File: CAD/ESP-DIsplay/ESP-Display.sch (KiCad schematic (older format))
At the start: 25 parts, among them J101 IO_Conn, J102 Conn_Power, SW101 SW_On, SW102 SW_Down, SW103 SW_Up, SW104 SW_T3, SW105 SW_T2, SW106 SW_T1, U101 SPI-TFT-1-8

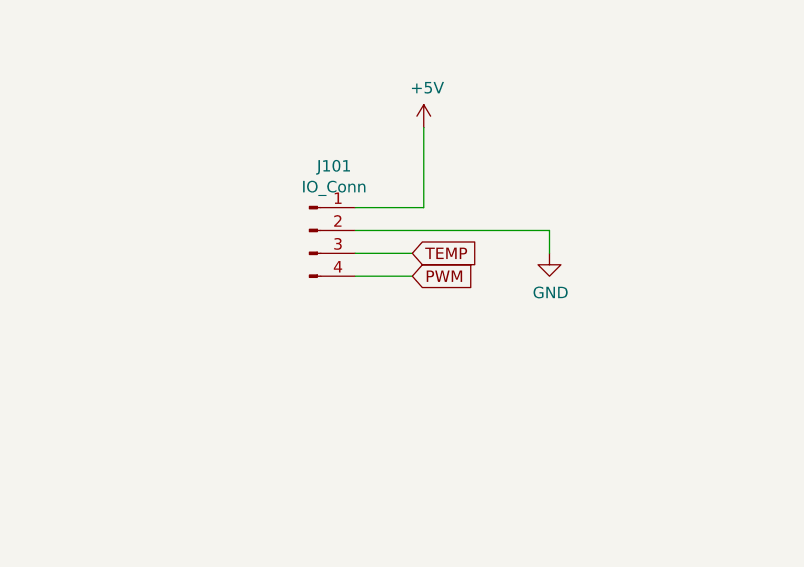
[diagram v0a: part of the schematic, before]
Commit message: esp12e adc pinsadded, 1117 power module
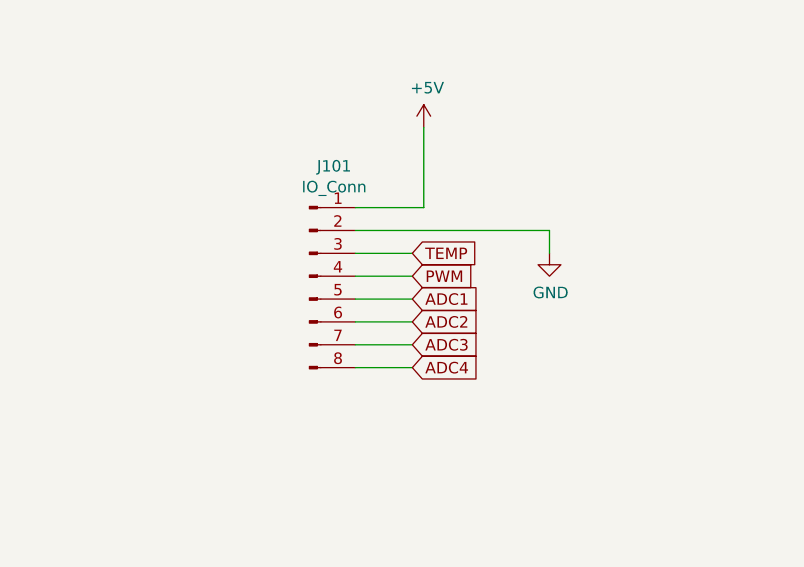
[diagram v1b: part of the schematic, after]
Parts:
- removed J101: IO_Conn, Connector_PinHeader_2.54mm:PinHeader_1x04_P2.54mm_Vertical, symbol Connector:Conn_01x04_Male
- added J101: IO_Conn, Connector_PinHeader_2.54mm:PinHeader_1x08_P2.54mm_Vertical, symbol Connector:Conn_01x08_Male
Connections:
- net labels added: ADC1, ADC2, ADC3, ADC4
- wire segments 65 -> 69
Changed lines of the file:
@@
-$EndComp
-$Comp
-L Connector:Conn_01x04_Male J101
-U 1 1 603BB008
-P 2150 5000
-F 0 "J101" H 2258 5281 50  0000 C CNN
-F 1 "IO_Conn" H 2258 5190 50  0000 C CNN
-F 2 "Connector_PinHeader_2.54mm:PinHeader_1x04_P2.54mm_Vertical" H 2150 5000 50  0001 C CNN
-F 3 "~" H 2150 5000 50  0001 C CNN
-	1    2150 5000
-	1    0    0    -1
 $EndComp
 $Comp
@@
 Wire Wire Line
 	6100 5100 6250 5100
+$Comp
+L Connector:Conn_01x08_Male J101
+U 1 1 603C3897
+P 2150 5200
+F 0 "J101" H 2258 5681 50  0000 C CNN
+F 1 "IO_Conn" H 2258 5590 50  0000 C CNN
+F 2 "Connector_PinHeader_2.54mm:PinHeader_1x08_P2.54mm_Vertical" H 2150 5200 50  0001 C CNN
+F 3 "~" H 2150 5200 50  0001 C CNN
+	1    2150 5200
+	1    0    0    -1
+$EndComp
+Text GLabel 2600 5300 2    50   Input ~ 0
+ADC1
+Text GLabel 2600 5400 2    50   Input ~ 0
+ADC2
+Text GLabel 2600 5500 2    50   Input ~ 0
+ADC3
+Text GLabel 2600 5600 2    50   Input ~ 0
+ADC4
+Wire Wire Line
+	2350 5300 2600 5300
+Wire Wire Line
+	2350 5400 2600 5400
+Wire Wire Line
+	2350 5500 2600 5500
+Wire Wire Line
+	2350 5600 2600 5600
 $EndSCHEMATC

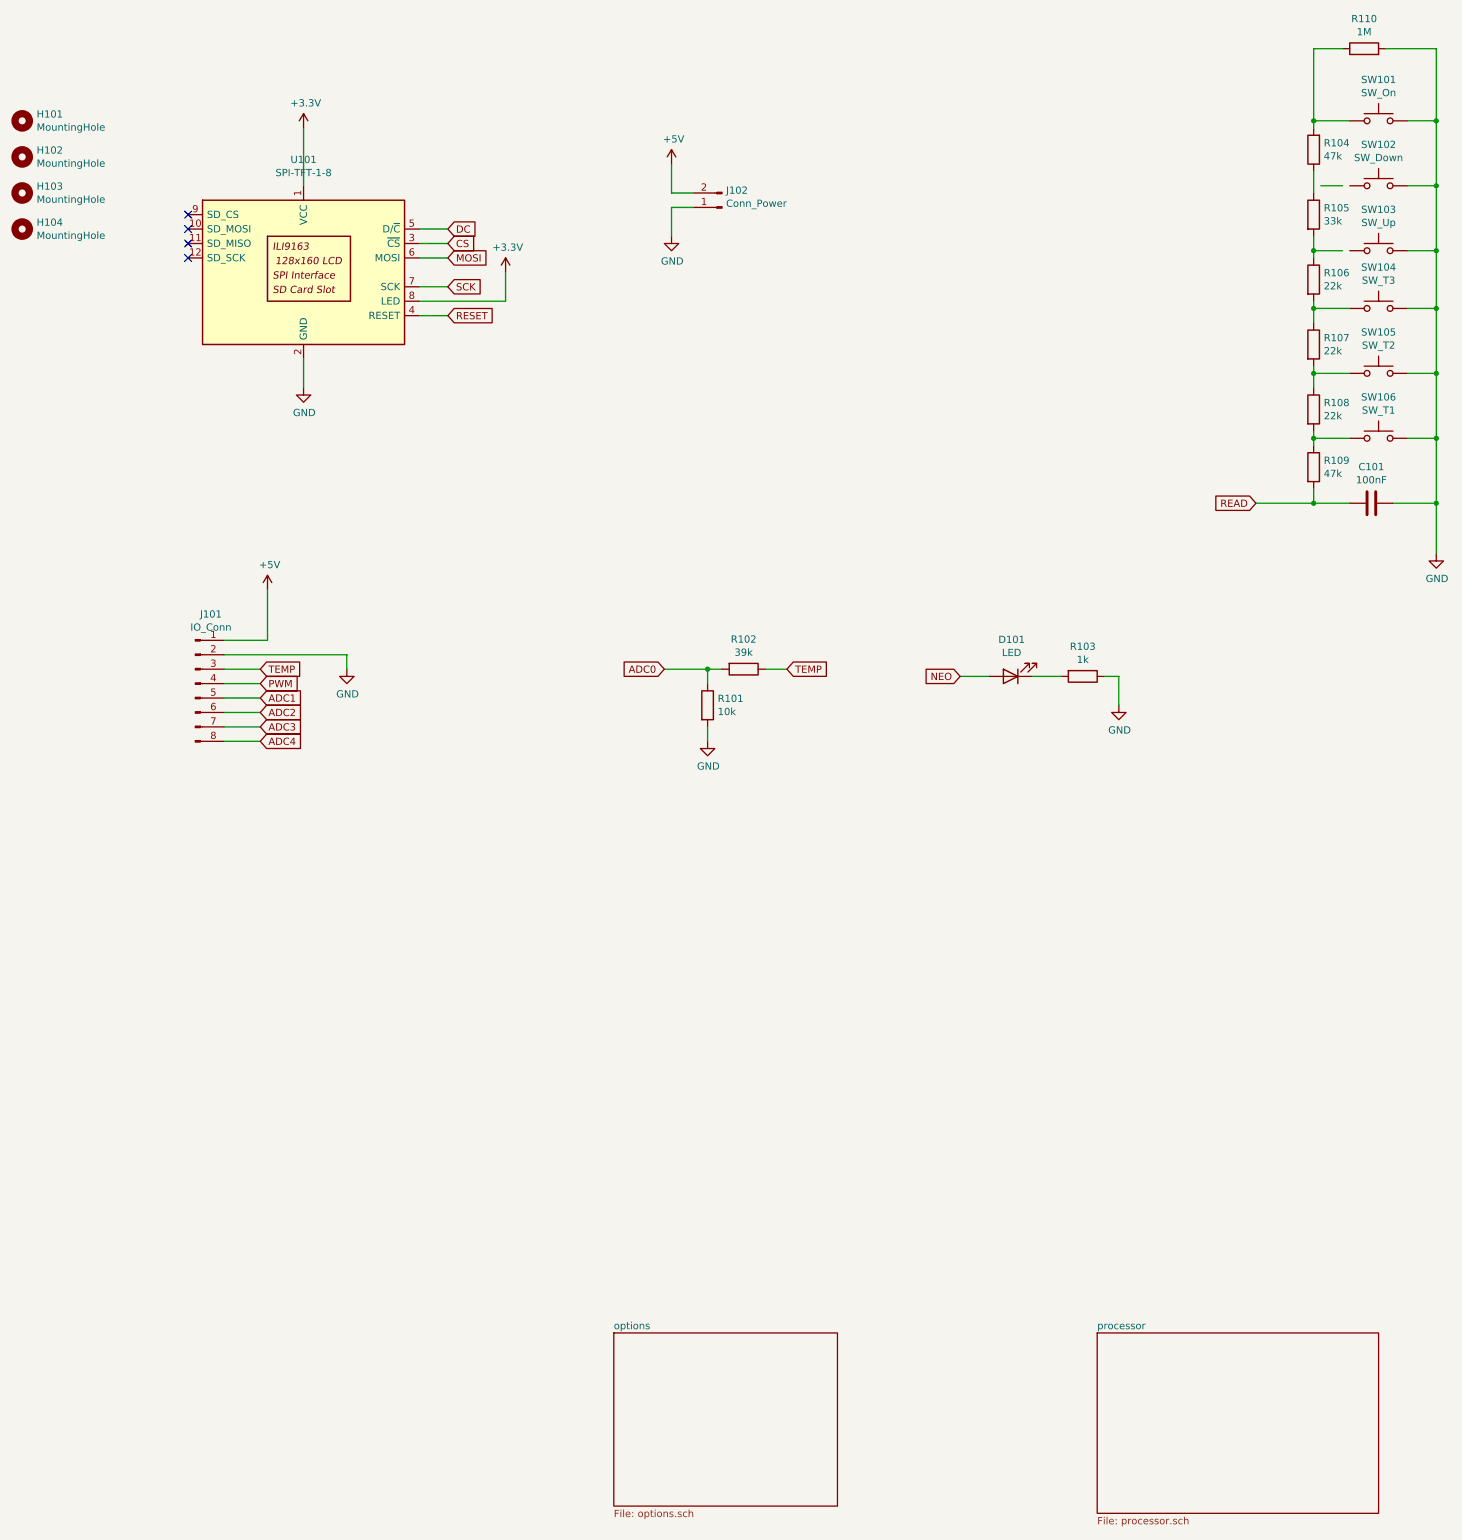
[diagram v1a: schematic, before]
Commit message: ESP32 added
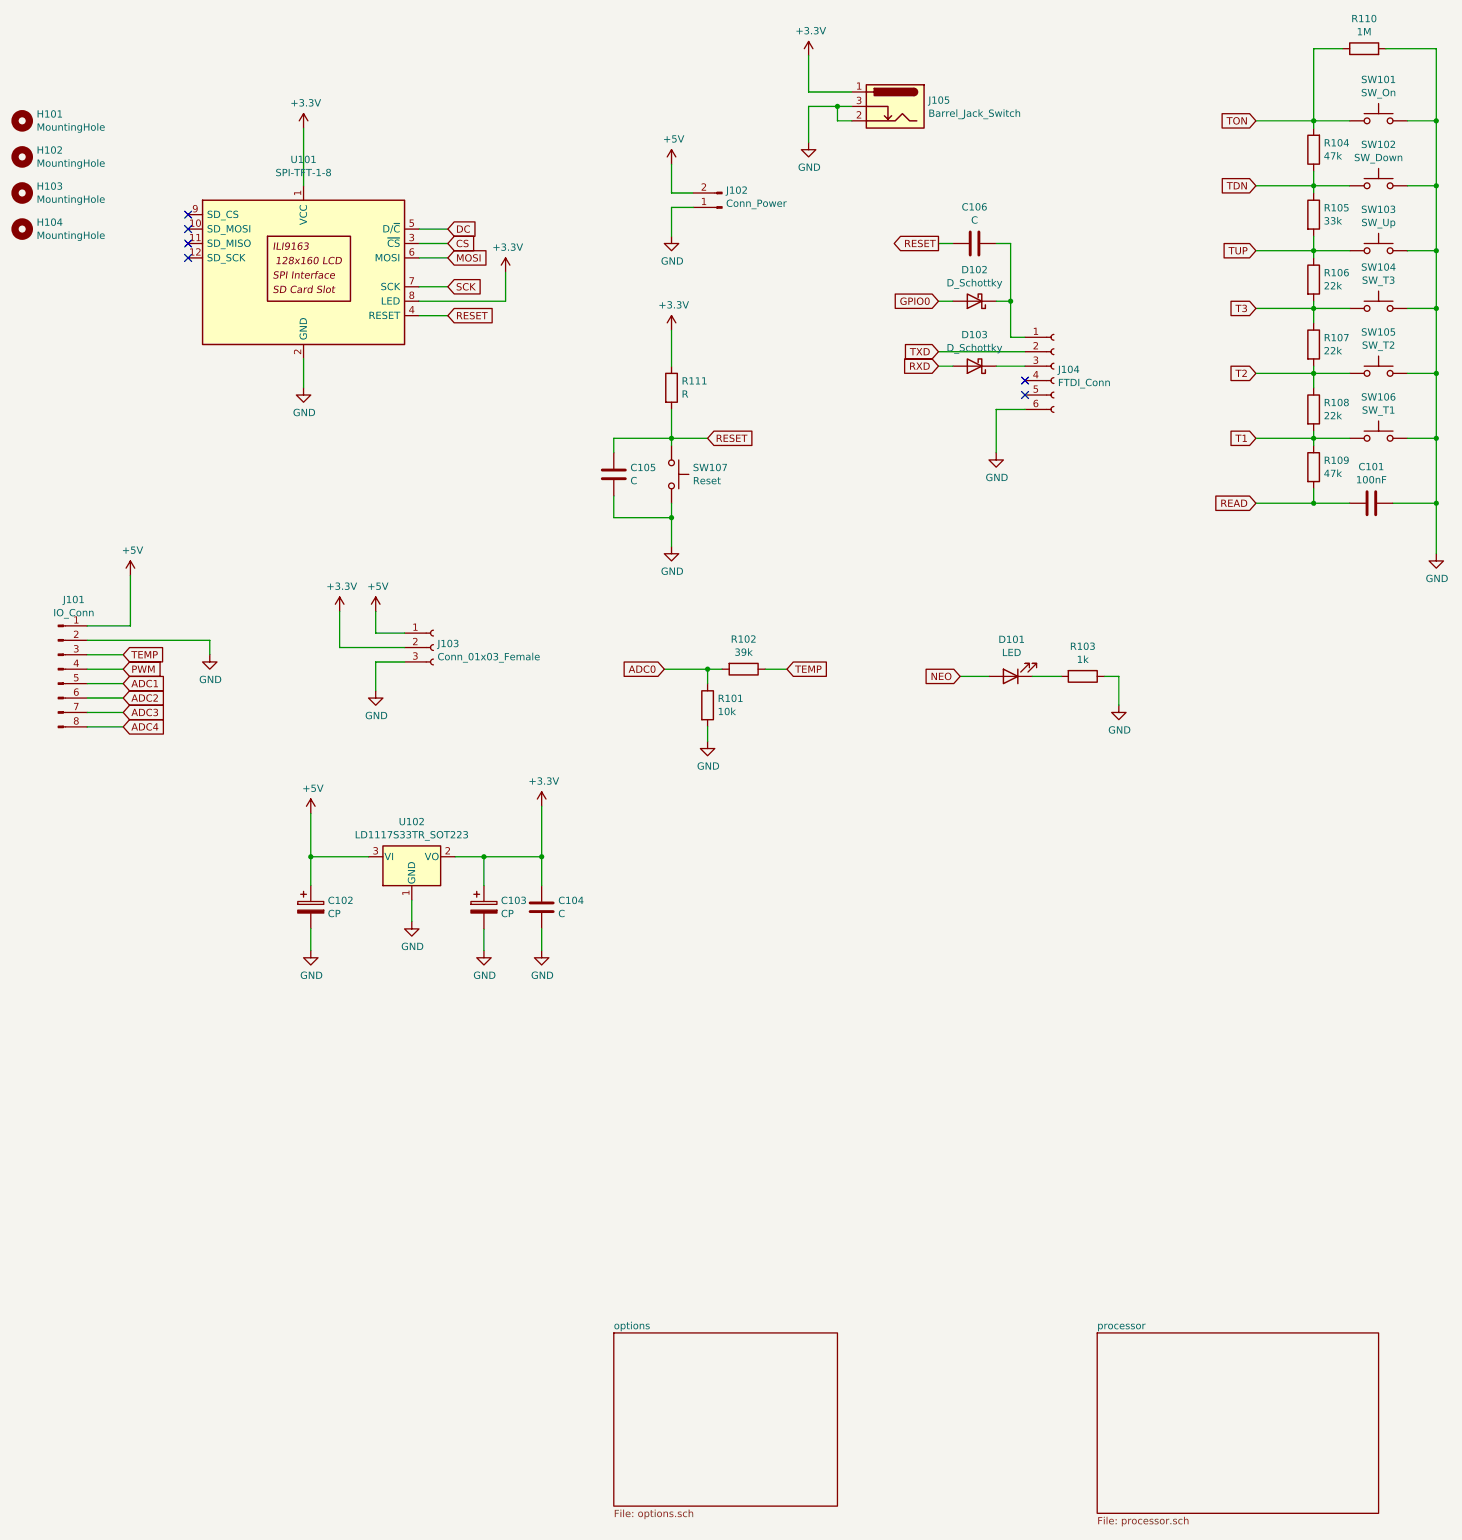
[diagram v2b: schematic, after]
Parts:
- added C102, C103: CP, Capacitor_Tantalum_SMD:CP_EIA-7343-15_Kemet-W, symbol Device:CP
- added C104, C105, C106: C, Capacitor_SMD:C_1206_3216Metric, symbol Device:C
- added D102, D103: D_Schottky, Diode_SMD:D_SOD-123, symbol Device:D_Schottky
- added J103: Conn_01x03_Female, Connector_PinSocket_2.54mm:PinSocket_1x03_P2.54mm_Vertical, symbol Connector:Conn_01x03_Female
- added J104: FTDI_Conn, Connector_PinSocket_2.54mm:PinSocket_1x06_P2.54mm_Vertical, symbol Connector:Conn_01x06_Female
- added J105: Barrel_Jack_Switch, Connector_BarrelJack:BarrelJack_Horizontal, symbol Connector:Barrel_Jack_Switch
- added R111: R, Resistor_SMD:R_0805_2012Metric, symbol Device:R
- added SW107: Reset, Button_Switch_THT:SW_PUSH_6mm_H5mm, symbol Switch:SW_Push
- added U102: LD1117S33TR_SOT223, Package_TO_SOT_SMD:SOT-223-3_TabPin2, symbol Regulator_Linear:LD1117S33TR_SOT223
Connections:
- net labels added: GPIO0, RXD, T1, T2, T3, TDN, TON, TUP, TXD
- wire segments 69 -> 123
- no-connect marks 4 -> 6
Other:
- moved on the sheet: J101

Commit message: ESP Display v1
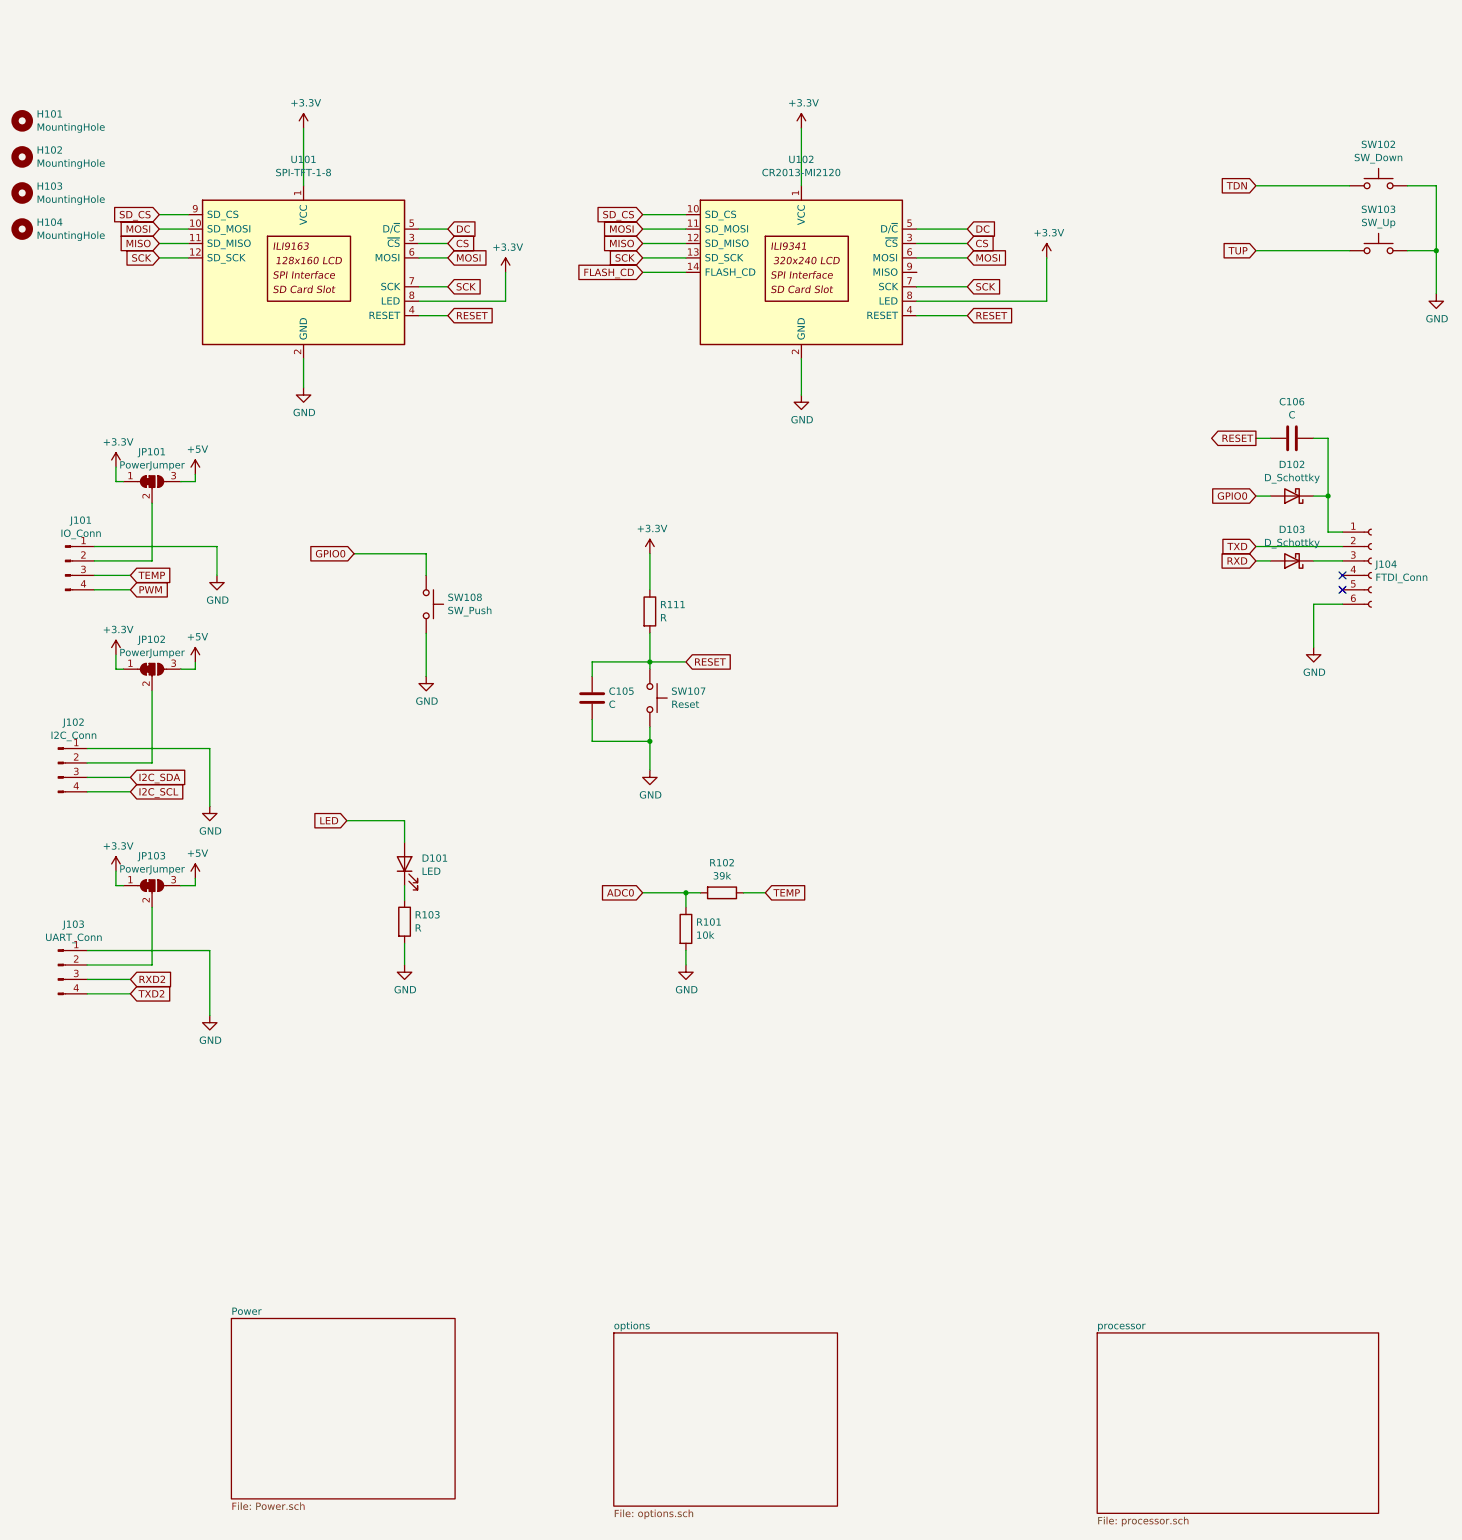
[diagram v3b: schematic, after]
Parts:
- removed C101: 100nF, Capacitor_SMD:C_1206_3216Metric, symbol Device:C
- removed C102, C103: CP, Capacitor_Tantalum_SMD:CP_EIA-7343-15_Kemet-W, symbol Device:CP
- removed C104: C, Capacitor_SMD:C_1206_3216Metric, symbol Device:C
- removed J101: IO_Conn, Connector_PinHeader_2.54mm:PinHeader_1x08_P2.54mm_Vertical, symbol Connector:Conn_01x08_Male
- removed J102: Conn_Power, Connector_JST:JST_XH_B2B-XH-AM_1x02_P2.50mm_Vertical, symbol Connector:Conn_01x02_Male
- removed J103: Conn_01x03_Female, Connector_PinSocket_2.54mm:PinSocket_1x03_P2.54mm_Vertical, symbol Connector:Conn_01x03_Female
- removed J105: Barrel_Jack_Switch, Connector_BarrelJack:BarrelJack_Horizontal, symbol Connector:Barrel_Jack_Switch
- removed R104, R109: 47k, Resistor_SMD:R_0805_2012Metric, symbol Device:R
- removed R105: 33k, Resistor_SMD:R_0805_2012Metric, symbol Device:R
- removed R106, R107, R108: 22k, Resistor_SMD:R_0805_2012Metric, symbol Device:R
- removed R110: 1M, Resistor_SMD:R_0805_2012Metric, symbol Device:R
- removed SW101: SW_On, Button_Switch_THT:SW_PUSH_6mm_H5mm, symbol Switch:SW_Push
- removed SW104: SW_T3, Button_Switch_THT:SW_PUSH_6mm_H5mm, symbol Switch:SW_Push
- removed SW105: SW_T2, Button_Switch_THT:SW_PUSH_6mm_H5mm, symbol Switch:SW_Push
- removed SW106: SW_T1, Button_Switch_THT:SW_PUSH_6mm_H5mm, symbol Switch:SW_Push
- removed U102: LD1117S33TR_SOT223, Package_TO_SOT_SMD:SOT-223-3_TabPin2, symbol Regulator_Linear:LD1117S33TR_SOT223
- added J101: IO_Conn, Connector_PinHeader_2.54mm:PinHeader_1x04_P2.54mm_Vertical, symbol Connector:Conn_01x04_Male
- added J102: I2C_Conn, Connector_PinHeader_2.54mm:PinHeader_1x04_P2.54mm_Vertical, symbol Connector:Conn_01x04_Male
- added J103: UART_Conn, Connector_PinHeader_2.54mm:PinHeader_1x04_P2.54mm_Vertical, symbol Connector:Conn_01x04_Male
- added JP101, JP102, JP103: PowerJumper, Jumper:SolderJumper-3_P1.3mm_Bridged12_Pad1.0x1.5mm, symbol Jumper:SolderJumper_3_Bridged12
- added SW108: SW_Push, Button_Switch_SMD:SW_Push_1P1T_NO_6x6mm_H9.5mm, symbol Switch:SW_Push
- added U102: CR2013-MI2120, Display:CR2013-MI2120, symbol MY_DISPLAY_DRIVER:CR2013-MI2120
- D101: footprint LED_THT:LED_D3.0mm_Clear -> LED_SMD:LED_1206_3216Metric
- R103: value 1k -> R
- SW107: footprint Button_Switch_THT:SW_PUSH_6mm_H5mm -> Button_Switch_SMD:SW_Push_1P1T_NO_6x6mm_H9.5mm
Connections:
- net +3V3: now also JP101.1 (A), JP102.1 (A), JP103.1 (A), U102.1 (VCC), U102.8 (LED)
- net +5V: now also JP101.3 (B), JP102.3 (B), JP103.3 (B)
- net CS: now also U102.3 (~CS)
- net DC: now also U102.5 (D/~C)
- net GND: now also R103.2, J101.1 (Pin_1), J102.1 (Pin_1), J103.1 (Pin_1), SW108.2, U102.2 (GND); no longer R103.1
- net GPIO0: now also SW108.1
- net MOSI: now also U101.10 (SD_MOSI), U102.11 (SD_MOSI), U102.6 (MOSI)
- net PWM: now also J101.4 (Pin_4)
- net RESET: now also U102.4 (RESET)
- net SCK: now also U101.12 (SD_SCK), U102.13 (SD_SCK), U102.7 (SCK)
- net TEMP: now also J101.3 (Pin_3)
- net MISO: now reaches U101.11 (SD_MISO)
- net MISO: now also U102.12 (SD_MISO)
- net SD_CS: now reaches U101.9 (SD_CS)
- net SD_CS: now also U102.10 (SD_CS)
- net at D101.1 (K): now also R103.1; no longer R103.2
- net NEO renamed LED
- new net: J101.2 (Pin_2), JP101.2 (C)
- new net: J102.2 (Pin_2), JP102.2 (C)
- new net: J103.2 (Pin_2), JP103.2 (C)
- new net FLASH_CD: U102.14 (FLASH_CD)
- new net I2C_SCL: J102.4 (Pin_4)
- new net I2C_SDA: J102.3 (Pin_3)
- new net RXD2: J103.3 (Pin_3)
- new net TXD2: J103.4 (Pin_4)
- no-connect marks 6 -> 2
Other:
- moved on the sheet: C105, C106, D102, D103, J104, R101, R102, R111, SW107
